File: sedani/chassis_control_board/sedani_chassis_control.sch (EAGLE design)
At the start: 27 parts, among them J1 WIRELESS E-STOP, J10 OUTPUT 2, J11 OUTPUT 3, J12 SELECT, J13 ENCODER INPUT, J14 RC SERVO INPUT, J15 RC ESC INPUT, J16 RC BUTTON INPUT, J17 AUDIO BOARD POWER, J18 AUDIO BOARD INPUT, J19 SERVO OUTPUT, J2 E-STOP INTERFACE, J20 ESC OUTPUT, J3 MASTER 1, J4 MASTER 2, J5 MASTER 3, J6 SLAVE 1, J7 SLAVE 2, J8 SLAVE 3, J9 OUTPUT 1, K1 EC2-5NU

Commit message: Corrected speaker enable to disable
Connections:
- net SPEAKER_ENABLE renamed SPEAKER_DISABLE
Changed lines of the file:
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@@
 </segment>
 </net>
-<net name="SPEAKER_ENABLE" class="0">
+<net name="SPEAKER_DISABLE" class="0">
 <segment>
 <pinref part="S1" gate="1" pin="S"/>

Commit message: Moved e-stop input routing for better connection
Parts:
- J17: SPICEPREFIX (none) -> J
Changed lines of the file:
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@@
 <part name="D2" library="SparkFun-DiscreteSemi" library_urn="urn:adsk.eagle:library:514" deviceset="DIODE" device="-BAS16J" package3d_urn="urn:adsk.eagle:package:38441/1" value="250mA/100V"/>
 <part name="D1" library="SparkFun-DiscreteSemi" library_urn="urn:adsk.eagle:library:514" deviceset="DIODE" device="-BAS16J" package3d_urn="urn:adsk.eagle:package:38441/1" value="250mA/100V"/>
-<part name="J17" library="SparkFun-Connectors" deviceset="CONN_03" device="" value="AUDIO BOARD POWER"/>
+<part name="J17" library="SparkFun-Connectors" deviceset="CONN_03" device="" value="AUDIO BOARD POWER">
+<attribute name="SPICEPREFIX" value="J"/>
+</part>
 <part name="SUPPLY4" library="SparkFun-PowerSymbols" deviceset="5V" device=""/>
 <part name="GND7" library="SparkFun-PowerSymbols" deviceset="GND" device=""/>

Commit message: ixed some stuff on the HW control board
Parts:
- added LED1: (no value), led:LED3MM
- added R1: 1k, rcl:R-US_R0603
- added R2: 10k, rcl:R-US_R0603
- added S2: KMR2, RoboJackets-Switches:KMR2
- added T1: 300mA, transistor:-NPN-SOT23-EBC
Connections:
- new net ARDUINO_RST: B1.RESET, R2.1, S2.2
- new net N$1: K1.8, T1.C
- new net N$2: K1.7, R1.1
- new net N$3: LED1.A, R1.2
- net 5V: now also K1.1, K1.6, R2.2
- net E-STOP_OUTPUT: now also T1.B; no longer K1.1
- net GND: now also K1.2, LED1.C, S2.1, T1.E; no longer K1.8
- net MUX_ESC: now also K1.4; no longer K1.3
- net OUT_ESC: now also K1.3; no longer K1.4
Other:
- moved on the sheet: G1

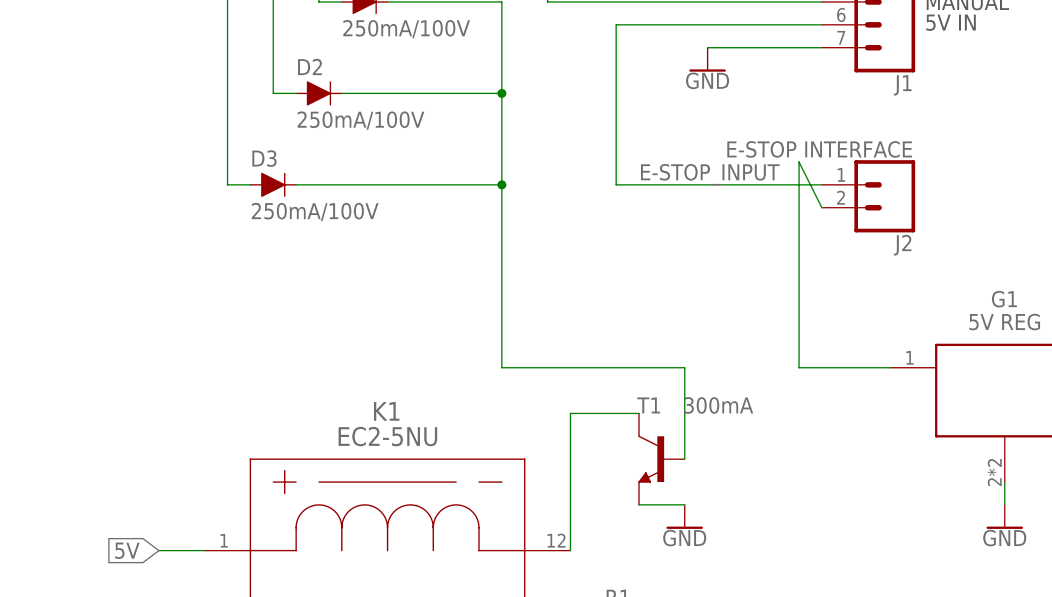
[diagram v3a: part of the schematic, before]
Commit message: added flyback diode and worked on routing
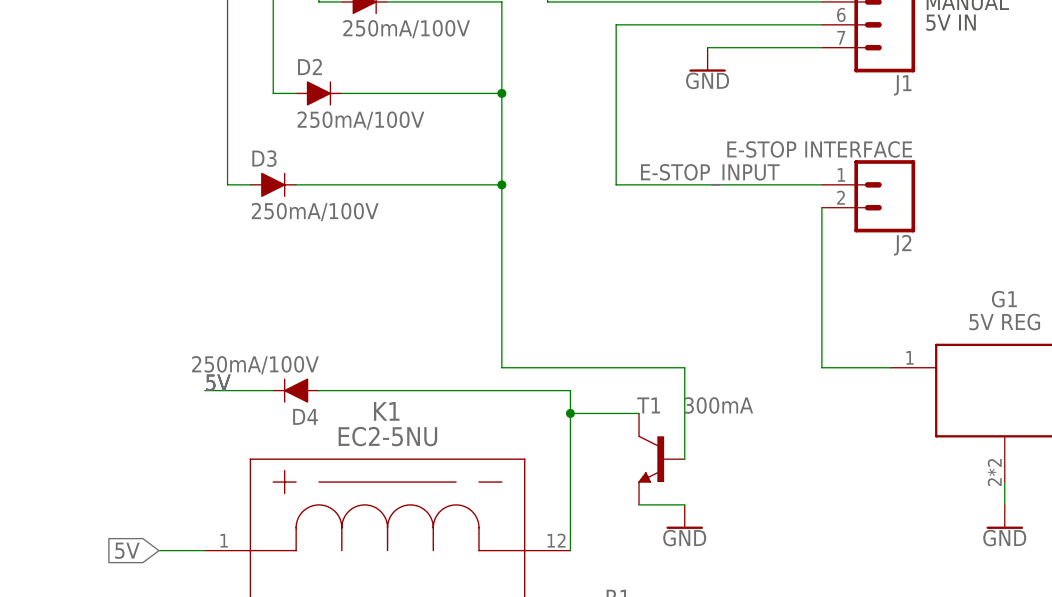
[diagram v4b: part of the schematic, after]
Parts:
- added D4: 250mA/100V, SparkFun-DiscreteSemi:DIODE-BAS16J
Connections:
- net ESC_5V renamed N$4
- net 5V: now also D4.C
- net N$1: now also D4.A
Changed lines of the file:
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@@
 <part name="GND11" library="SparkFun-PowerSymbols" deviceset="GND" device=""/>
 <part name="FRAME1" library="RoboJackets-Frames" deviceset="FRAME_B_L" device="">
-<attribute name="REVISION" value="3.0"/>
+<attribute name="REVISION" value="3.1"/>
 <attribute name="TEAM" value="RoboRacing"/>
 </part>
@@
 <part name="GND13" library="SparkFun-PowerSymbols" deviceset="GND" device=""/>
 <part name="R2" library="rcl" library_urn="urn:adsk.eagle:library:334" deviceset="R-US_" device="R0603" package3d_urn="urn:adsk.eagle:package:23555/2" value="10k"/>
+<part name="D4" library="SparkFun-DiscreteSemi" library_urn="urn:adsk.eagle:library:514" deviceset="DIODE" device="-BAS16J" package3d_urn="urn:adsk.eagle:package:38441/1" value="250mA/100V"/>
 </parts>
 <sheets>
@@
 <attribute name="NAME" x="95.25" y="110.7186" size="1.778" layer="95"/>
 <attribute name="VALUE" x="95.25" y="105.918" size="1.778" layer="96"/>
+</instance>
+<instance part="D4" gate="G$1" x="45.72" y="200.66" smashed="yes" rot="R180">
+<attribute name="NAME" x="48.26" y="198.628" size="1.778" layer="95" font="vector" rot="R180"/>
+<attribute name="VALUE" x="48.26" y="202.692" size="1.778" layer="96" font="vector" rot="R180" align="top-left"/>
 </instance>
 </instances>
@@
 </segment>
 <segment>
-<pinref part="K1" gate="A" pin="1"/>
-<wire x1="30.48" y1="182.88" x2="35.56" y2="182.88" width="0.1524" layer="91"/>
-<label x="30.48" y="182.88" size="1.778" layer="95" rot="R180" xref="yes"/>
+<pinref part="D4" gate="G$1" pin="C"/>
+<wire x1="35.56" y1="200.66" x2="43.18" y2="200.66" width="0.1524" layer="91"/>
+<label x="35.56" y="200.66" size="1.778" layer="95"/>
+<label x="35.56" y="200.66" size="1.778" layer="95"/>
 </segment>
 <segment>
@@
 <wire x1="104.14" y1="109.22" x2="106.68" y2="109.22" width="0.1524" layer="91"/>
 <label x="106.68" y="109.22" size="1.778" layer="95" xref="yes"/>
+</segment>
+<segment>
+<pinref part="K1" gate="A" pin="1"/>
+<wire x1="30.48" y1="182.88" x2="35.56" y2="182.88" width="0.1524" layer="91"/>
+<label x="30.48" y="182.88" size="1.778" layer="95" rot="R180" xref="yes"/>
 </segment>
 </net>
@@
 <wire x1="50.8" y1="243.84" x2="48.26" y2="243.84" width="0.1524" layer="91"/>
 <wire x1="48.26" y1="243.84" x2="48.26" y2="248.92" width="0.1524" layer="91"/>
-</segment>
-</net>
-<net name="ESC_5V" class="0">
-<segment>
-<pinref part="G1" gate="A" pin="OUTPUT"/>
-<wire x1="111.76" y1="203.2" x2="101.6" y2="203.2" width="0.1524" layer="91"/>
-<pinref part="J2" gate="G$1" pin="2"/>
-<wire x1="101.6" y1="203.2" x2="101.6" y2="226.06" width="0.1524" layer="91"/>
-<wire x1="101.6" y1="226.06" x2="104.14" y2="220.98" width="0.1524" layer="91"/>
 </segment>
 </net>
@@
 <pinref part="T1" gate="G$1" pin="C"/>
 <wire x1="76.2" y1="198.12" x2="83.82" y2="198.12" width="0.1524" layer="91"/>
+<pinref part="D4" gate="G$1" pin="A"/>
+<wire x1="48.26" y1="200.66" x2="76.2" y2="200.66" width="0.1524" layer="91"/>
+<wire x1="76.2" y1="200.66" x2="76.2" y2="198.12" width="0.1524" layer="91"/>
+<junction x="76.2" y="198.12"/>
 </segment>
 </net>
@@
 </segment>
 </net>
+<net name="N$4" class="0">
+<segment>
+<pinref part="J2" gate="G$1" pin="2"/>
+<pinref part="G1" gate="A" pin="OUTPUT"/>
+<wire x1="104.14" y1="220.98" x2="104.14" y2="203.2" width="0.1524" layer="91"/>
+<wire x1="104.14" y1="203.2" x2="111.76" y2="203.2" width="0.1524" layer="91"/>
+</segment>
+</net>

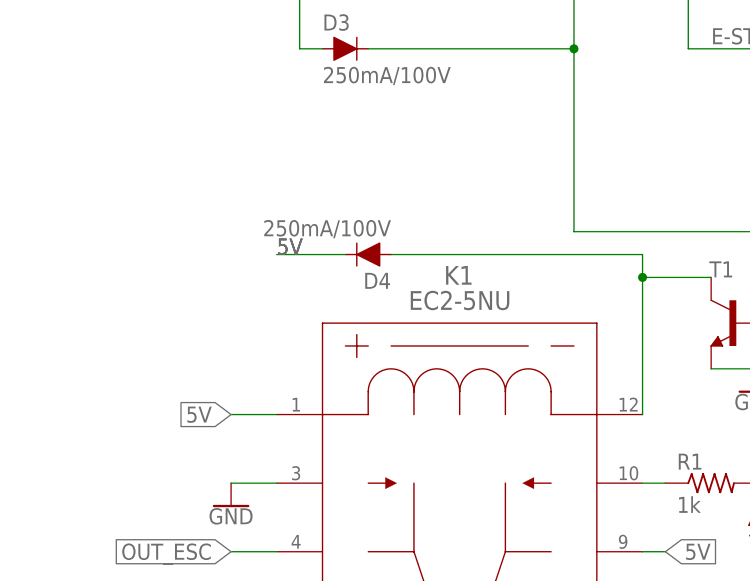
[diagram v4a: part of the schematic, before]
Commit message: Clarified flyback diode configuration
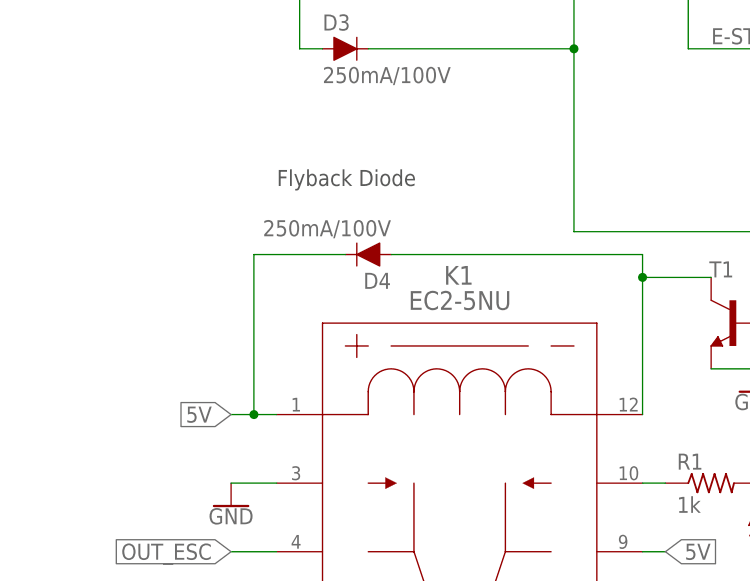
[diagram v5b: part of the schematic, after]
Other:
- note added: "Flyback Diode"
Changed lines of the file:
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@@
 <text x="115.57" y="243.84" size="1.778" layer="97" align="center-left">MANUAL</text>
 <text x="115.57" y="241.554" size="1.778" layer="97" align="center-left">5V IN</text>
+<text x="35.56" y="208.28" size="1.778" layer="97">Flyback Diode</text>
 </plain>
 <instances>
@@
 <segment>
 <pinref part="D4" gate="G$1" pin="C"/>
-<wire x1="35.56" y1="200.66" x2="43.18" y2="200.66" width="0.1524" layer="91"/>
-<label x="35.56" y="200.66" size="1.778" layer="95"/>
-<label x="35.56" y="200.66" size="1.778" layer="95"/>
+<wire x1="33.02" y1="200.66" x2="43.18" y2="200.66" width="0.1524" layer="91"/>
+<pinref part="K1" gate="A" pin="1"/>
+<wire x1="30.48" y1="182.88" x2="33.02" y2="182.88" width="0.1524" layer="91"/>
+<label x="30.48" y="182.88" size="1.778" layer="95" rot="R180" xref="yes"/>
+<wire x1="33.02" y1="182.88" x2="35.56" y2="182.88" width="0.1524" layer="91"/>
+<wire x1="33.02" y1="200.66" x2="33.02" y2="182.88" width="0.1524" layer="91"/>
+<junction x="33.02" y="182.88"/>
 </segment>
 <segment>
@@
 <label x="106.68" y="109.22" size="1.778" layer="95" xref="yes"/>
 </segment>
-<segment>
-<pinref part="K1" gate="A" pin="1"/>
-<wire x1="30.48" y1="182.88" x2="35.56" y2="182.88" width="0.1524" layer="91"/>
-<label x="30.48" y="182.88" size="1.778" layer="95" rot="R180" xref="yes"/>
-</segment>
 </net>

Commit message: started E-stop rebuild
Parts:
- removed D4: 250mA/100V, SparkFun-DiscreteSemi:DIODE-BAS16J
- removed K1: EC2-5NU, sedani_chassis_control:EC2-5NU
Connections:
- net ENCODER_A renamed SPEED_A
- net ENCODER_B renamed SPEED_B
- removed net MUX_ESC: J10.3, K1.4
- removed net N$2: K1.7, R1.1
- net 5V: no longer D4.C, K1.1, K1.6
- net GND: no longer K1.2, LED1.C
- net N$1: now also LED1.C; no longer D4.A, K1.8
- net OUT_ESC: now also J10.3; no longer K1.3
- net VCC: now also R1.1
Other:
- note removed: "Flyback Diode"
- moved on the sheet: LED1, R1
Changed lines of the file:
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@@
 <part name="SUPPLY4" library="SparkFun-PowerSymbols" deviceset="5V" device=""/>
 <part name="GND7" library="SparkFun-PowerSymbols" deviceset="GND" device=""/>
-<part name="K1" library="sedani_chassis_control" deviceset="EC2-5NU" device=""/>
 <part name="G1" library="hw_interface_board" deviceset="VOLTAGE_REG" device="" value="5V REG"/>
 <part name="RCVCC3" library="SparkFun-PowerSymbols" deviceset="VCC" device=""/>
@@
 <part name="T1" library="transistor" library_urn="urn:adsk.eagle:library:402" deviceset="*-NPN-" device="SOT23-EBC" package3d_urn="urn:adsk.eagle:package:29920/2" value="300mA"/>
 <part name="GND8" library="SparkFun-PowerSymbols" deviceset="GND" device=""/>
-<part name="GND9" library="SparkFun-PowerSymbols" deviceset="GND" device=""/>
 <part name="LED1" library="led" library_urn="urn:adsk.eagle:library:259" deviceset="LED" device="3MM" package3d_urn="urn:adsk.eagle:package:15797/1"/>
-<part name="GND12" library="SparkFun-PowerSymbols" deviceset="GND" device=""/>
 <part name="R1" library="rcl" library_urn="urn:adsk.eagle:library:334" deviceset="R-US_" device="R0603" package3d_urn="urn:adsk.eagle:package:23555/2" value="1k"/>
 <part name="S2" library="RoboJackets-Switches" deviceset="KMR2" device=""/>
 <part name="GND13" library="SparkFun-PowerSymbols" deviceset="GND" device=""/>
 <part name="R2" library="rcl" library_urn="urn:adsk.eagle:library:334" deviceset="R-US_" device="R0603" package3d_urn="urn:adsk.eagle:package:23555/2" value="10k"/>
-<part name="D4" library="SparkFun-DiscreteSemi" library_urn="urn:adsk.eagle:library:514" deviceset="DIODE" device="-BAS16J" package3d_urn="urn:adsk.eagle:package:38441/1" value="250mA/100V"/>
+<part name="RCVCC4" library="SparkFun-PowerSymbols" deviceset="VCC" device=""/>
 </parts>
 <sheets>
@@
 <text x="115.57" y="243.84" size="1.778" layer="97" align="center-left">MANUAL</text>
 <text x="115.57" y="241.554" size="1.778" layer="97" align="center-left">5V IN</text>
-<text x="35.56" y="208.28" size="1.778" layer="97">Flyback Diode</text>
 </plain>
 <instances>
@@
 <instance part="GND7" gate="1" x="215.9" y="83.82" smashed="yes" rot="R90">
 <attribute name="VALUE" x="216.154" y="83.82" size="1.778" layer="96" rot="R90" align="top-center"/>
-</instance>
-<instance part="K1" gate="A" x="55.88" y="175.26" smashed="yes">
-<attribute name="NAME" x="55.7784" y="198.3486" size="2.0828" layer="95" ratio="6" rot="SMR0" align="center"/>
-<attribute name="VALUE" x="55.9054" y="195.5546" size="2.0828" layer="96" ratio="6" rot="SMR0" align="center"/>
 </instance>
 <instance part="G1" gate="A" x="124.46" y="203.2" smashed="yes">
@@
 <attribute name="VALUE" x="88.9" y="185.166" size="1.778" layer="96" align="top-center"/>
 </instance>
-<instance part="GND9" gate="1" x="30.48" y="172.72" smashed="yes">
-<attribute name="VALUE" x="30.48" y="172.466" size="1.778" layer="96" align="top-center"/>
-</instance>
-<instance part="LED1" gate="G$1" x="91.44" y="172.72" smashed="yes">
-<attribute name="NAME" x="94.996" y="168.148" size="1.778" layer="95" rot="R90"/>
-<attribute name="VALUE" x="97.155" y="168.148" size="1.778" layer="96" rot="R90"/>
-</instance>
-<instance part="GND12" gate="1" x="91.44" y="162.56" smashed="yes">
-<attribute name="VALUE" x="91.44" y="162.306" size="1.778" layer="96" align="top-center"/>
-</instance>
-<instance part="R1" gate="G$1" x="83.82" y="175.26" smashed="yes">
-<attribute name="NAME" x="80.01" y="176.7586" size="1.778" layer="95"/>
-<attribute name="VALUE" x="80.01" y="171.958" size="1.778" layer="96"/>
+<instance part="LED1" gate="G$1" x="66.04" y="198.12" smashed="yes" rot="R90">
+<attribute name="NAME" x="70.612" y="201.676" size="1.778" layer="95" rot="R180"/>
+<attribute name="VALUE" x="70.612" y="203.835" size="1.778" layer="96" rot="R180"/>
+</instance>
+<instance part="R1" gate="G$1" x="55.88" y="198.12" smashed="yes">
+<attribute name="NAME" x="52.07" y="199.6186" size="1.778" layer="95"/>
+<attribute name="VALUE" x="52.07" y="194.818" size="1.778" layer="96"/>
 </instance>
 <instance part="S2" gate="G$1" x="86.36" y="101.6" smashed="yes">
@@
 <attribute name="VALUE" x="95.25" y="105.918" size="1.778" layer="96"/>
 </instance>
-<instance part="D4" gate="G$1" x="45.72" y="200.66" smashed="yes" rot="R180">
-<attribute name="NAME" x="48.26" y="198.628" size="1.778" layer="95" font="vector" rot="R180"/>
-<attribute name="VALUE" x="48.26" y="202.692" size="1.778" layer="96" font="vector" rot="R180" align="top-left"/>
+<instance part="RCVCC4" gate="G$1" x="45.72" y="198.12" smashed="yes" rot="R90">
+<attribute name="VALUE" x="42.926" y="198.12" size="1.778" layer="96" rot="R180" align="bottom-center"/>
 </instance>
 </instances>
@@
 </segment>
 <segment>
-<pinref part="GND9" gate="1" pin="GND"/>
-<pinref part="K1" gate="A" pin="2"/>
-<wire x1="30.48" y1="175.26" x2="35.56" y2="175.26" width="0.1524" layer="91"/>
-</segment>
-<segment>
-<pinref part="LED1" gate="G$1" pin="C"/>
-<pinref part="GND12" gate="1" pin="GND"/>
-<wire x1="91.44" y1="167.64" x2="91.44" y2="165.1" width="0.1524" layer="91"/>
-</segment>
-<segment>
 <pinref part="GND13" gate="1" pin="GND"/>
 <pinref part="S2" gate="G$1" pin="1"/>
@@
 <pinref part="RCVCC3" gate="G$1" pin="VCC"/>
 </segment>
+<segment>
+<pinref part="RCVCC4" gate="G$1" pin="VCC"/>
+<pinref part="R1" gate="G$1" pin="1"/>
+<wire x1="45.72" y1="198.12" x2="50.8" y2="198.12" width="0.1524" layer="91"/>
+</segment>
 </net>
 <net name="MUX_SEL_READ" class="0">
@@
 </segment>
 <segment>
-<pinref part="D4" gate="G$1" pin="C"/>
-<wire x1="33.02" y1="200.66" x2="43.18" y2="200.66" width="0.1524" layer="91"/>
-<pinref part="K1" gate="A" pin="1"/>
-<wire x1="30.48" y1="182.88" x2="33.02" y2="182.88" width="0.1524" layer="91"/>
-<label x="30.48" y="182.88" size="1.778" layer="95" rot="R180" xref="yes"/>
-<wire x1="33.02" y1="182.88" x2="35.56" y2="182.88" width="0.1524" layer="91"/>
-<wire x1="33.02" y1="200.66" x2="33.02" y2="182.88" width="0.1524" layer="91"/>
-<junction x="33.02" y="182.88"/>
-</segment>
-<segment>
-<pinref part="K1" gate="A" pin="6"/>
-<wire x1="76.2" y1="167.64" x2="78.74" y2="167.64" width="0.1524" layer="91"/>
-<label x="78.74" y="167.64" size="1.778" layer="95" xref="yes"/>
-</segment>
-<segment>
 <pinref part="B1" gate="G$1" pin="VCC"/>
 <wire x1="88.9" y1="63.5" x2="101.6" y2="63.5" width="0.1524" layer="91"/>
@@
 </segment>
 </net>
-<net name="ENCODER_A" class="0">
+<net name="SPEED_A" class="0">
 <segment>
 <pinref part="J13" gate="G$1" pin="2"/>
@@
 </segment>
 </net>
-<net name="ENCODER_B" class="0">
+<net name="SPEED_B" class="0">
 <segment>
 <pinref part="J13" gate="G$1" pin="4"/>
@@
 </segment>
 <segment>
-<pinref part="K1" gate="A" pin="3"/>
-<label x="30.48" y="167.64" size="1.778" layer="95" rot="R180" xref="yes"/>
-<wire x1="30.48" y1="167.64" x2="35.56" y2="167.64" width="0.1524" layer="91"/>
+<pinref part="J10" gate="J$1" pin="3"/>
+<wire x1="292.1" y1="226.06" x2="289.56" y2="226.06" width="0.1524" layer="91"/>
+<label x="289.56" y="226.06" size="1.778" layer="95" rot="R180" xref="yes"/>
 </segment>
 </net>
@@
 <wire x1="50.8" y1="243.84" x2="48.26" y2="243.84" width="0.1524" layer="91"/>
 <wire x1="48.26" y1="243.84" x2="48.26" y2="248.92" width="0.1524" layer="91"/>
-</segment>
-</net>
-<net name="MUX_ESC" class="0">
-<segment>
-<pinref part="J10" gate="J$1" pin="3"/>
-<wire x1="292.1" y1="226.06" x2="289.56" y2="226.06" width="0.1524" layer="91"/>
-<label x="289.56" y="226.06" size="1.778" layer="95" rot="R180" xref="yes"/>
-</segment>
-<segment>
-<pinref part="K1" gate="A" pin="4"/>
-<wire x1="35.56" y1="160.02" x2="30.48" y2="160.02" width="0.1524" layer="91"/>
-<label x="30.48" y="160.02" size="1.778" layer="95" rot="R180" xref="yes"/>
 </segment>
 </net>
@@
 </segment>
 </net>
-<net name="N$2" class="0">
-<segment>
-<pinref part="K1" gate="A" pin="7"/>
-<pinref part="R1" gate="G$1" pin="1"/>
-<wire x1="76.2" y1="175.26" x2="78.74" y2="175.26" width="0.1524" layer="91"/>
-</segment>
-</net>
 <net name="N$3" class="0">
 <segment>
 <pinref part="R1" gate="G$1" pin="2"/>
 <pinref part="LED1" gate="G$1" pin="A"/>
-<wire x1="88.9" y1="175.26" x2="91.44" y2="175.26" width="0.1524" layer="91"/>
-</segment>
-</net>
-<net name="N$1" class="0">
-<segment>
-<pinref part="K1" gate="A" pin="8"/>
-<wire x1="76.2" y1="182.88" x2="76.2" y2="198.12" width="0.1524" layer="91"/>
-<pinref part="T1" gate="G$1" pin="C"/>
-<wire x1="76.2" y1="198.12" x2="83.82" y2="198.12" width="0.1524" layer="91"/>
-<pinref part="D4" gate="G$1" pin="A"/>
-<wire x1="48.26" y1="200.66" x2="76.2" y2="200.66" width="0.1524" layer="91"/>
-<wire x1="76.2" y1="200.66" x2="76.2" y2="198.12" width="0.1524" layer="91"/>
-<junction x="76.2" y="198.12"/>
+<wire x1="60.96" y1="198.12" x2="63.5" y2="198.12" width="0.1524" layer="91"/>
 </segment>
 </net>
@@
 </segment>
 </net>
+<net name="N$1" class="0">
+<segment>
+<pinref part="LED1" gate="G$1" pin="C"/>
+<pinref part="T1" gate="G$1" pin="C"/>
+<wire x1="71.12" y1="198.12" x2="83.82" y2="198.12" width="0.1524" layer="91"/>
+</segment>
+</net>
